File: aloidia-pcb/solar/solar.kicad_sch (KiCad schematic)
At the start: 4 parts, among them J1 S2B-PH-SM4-TB(LF)(SN)

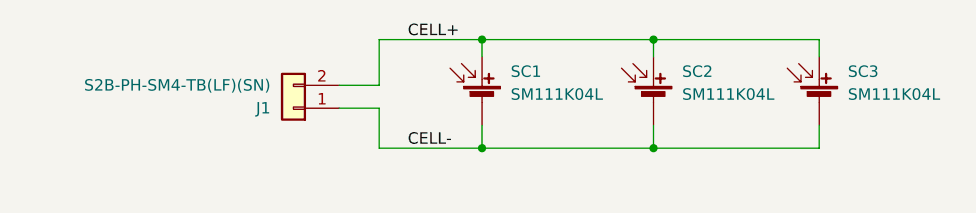
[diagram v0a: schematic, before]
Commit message: Changed connectors to jst-sh
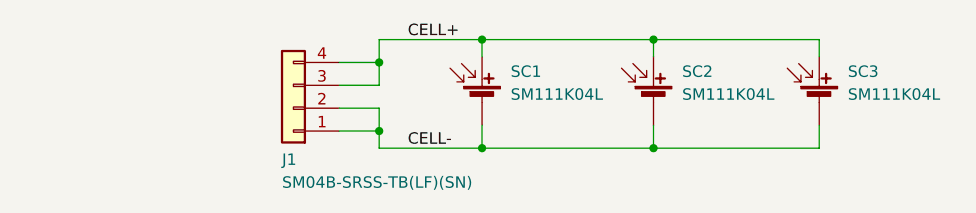
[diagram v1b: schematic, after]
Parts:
- removed J1: S2B-PH-SM4-TB(LF)(SN), Connector_JST:JST_PH_S2B-PH-SM4-TB_1x02-1MP_P2.00mm_Horizontal, symbol Connector_Generic:Conn_01x02
- added J1: SM04B-SRSS-TB(LF)(SN), Connector_JST:JST_SH_SM04B-SRSS-TB_1x04-1MP_P1.00mm_Horizontal, symbol Connector_Generic:Conn_01x04
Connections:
- net CELL+: now also J1.3 (Pin_3), J1.4 (Pin_4)
- net CELL-: now also J1.1 (Pin_1), J1.2 (Pin_2)
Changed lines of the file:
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@@
     (comment 2 "Author: Vincent Nguyen")
+  )
+  (junction (at 130.81 94.615) (diameter 0) (color 0 0 0 0)
+  )
+  (junction (at 130.81 102.235) (diameter 0) (color 0 0 0 0)
   )
   (junction (at 142.24 92.075) (diameter 0) (color 0 0 0 0)
@@
   )
   (junction (at 161.29 104.14) (diameter 0) (color 0 0 0 0)
+  )
+  (wire (pts (xy 126.365 102.235) (xy 130.81 102.235))
+    (stroke (width 0) (type default) (color 0 0 0 0))
   )
   (wire (pts (xy 161.29 92.075) (xy 179.705 92.075))
@@
     (stroke (width 0) (type default) (color 0 0 0 0))
   )
-  (wire (pts (xy 130.81 97.155) (xy 130.81 92.075))
+  (wire (pts (xy 130.81 92.075) (xy 130.81 94.615))
     (stroke (width 0) (type default) (color 0 0 0 0))
   )
@@
   )
   (wire (pts (xy 179.705 101.6) (xy 179.705 104.14))
+    (stroke (width 0) (type default) (color 0 0 0 0))
+  )
+  (wire (pts (xy 126.365 94.615) (xy 130.81 94.615))
     (stroke (width 0) (type default) (color 0 0 0 0))
   )
@@
     (stroke (width 0) (type default) (color 0 0 0 0))
   )
-  (wire (pts (xy 130.81 99.695) (xy 130.81 104.14))
+  (wire (pts (xy 130.81 99.695) (xy 130.81 102.235))
+    (stroke (width 0) (type default) (color 0 0 0 0))
+  )
+  (wire (pts (xy 130.81 94.615) (xy 130.81 97.155))
+    (stroke (width 0) (type default) (color 0 0 0 0))
+  )
+  (wire (pts (xy 130.81 102.235) (xy 130.81 104.14))
     (stroke (width 0) (type default) (color 0 0 0 0))
   )
@@
     (pin "2")
   )
-  (symbol (lib_id "Connector_Generic:Conn_01x02") (at 121.285 99.695 180) (unit 1)
-    (in_bom yes) (on_board yes) (fields_autoplaced)
-    (property "Reference" "J1" (id 0) (at 118.745 99.6951 0)
-      (effects (font (size 1.27 1.27)) (justify left))
+  (symbol (lib_id "Connector_Generic:Conn_01x04") (at 121.285 99.695 180) (unit 1)
+    (in_bom yes) (on_board yes)
+    (property "Reference" "J1" (id 0) (at 120.015 105.41 0)
+      (effects (font (size 1.27 1.27)) (justify right))
     )
-    (property "Value" "S2B-PH-SM4-TB(LF)(SN)" (id 1) (at 118.745 97.1551 0)
-      (effects (font (size 1.27 1.27)) (justify left))
+    (property "Value" "SM04B-SRSS-TB(LF)(SN)" (id 1) (at 120.015 107.95 0)
+      (effects (font (size 1.27 1.27)) (justify right))
     )
-    (property "Footprint" "Connector_JST:JST_PH_S2B-PH-SM4-TB_1x02-1MP_P2.00mm_Horizontal" (id 2) (at 121.285 99.695 0)
+    (property "Footprint" "Connector_JST:JST_SH_SM04B-SRSS-TB_1x04-1MP_P1.00mm_Horizontal" (id 2) (at 121.285 99.695 0)
       (effects (font (size 1.27 1.27)) hide)
     )
@@
     (pin "1")
     (pin "2")
+    (pin "3")
+    (pin "4")
   )
   (symbol (lib_id "Device:Solar_Cell") (at 179.705 99.06 0) (unit 1)
@@
   )
   (symbol_instances
-    (path "/dd7481c5-e18b-4131-a3de-fb23c40c0bf5"
-      (reference "J1") (unit 1) (value "S2B-PH-SM4-TB(LF)(SN)") (footprint "Connector_JST:JST_PH_S2B-PH-SM4-TB_1x02-1MP_P2.00mm_Horizontal")
+    (path "/b829a62e-8f9e-48dc-83b9-c62a484abb2a"
+      (reference "J1") (unit 1) (value "SM04B-SRSS-TB(LF)(SN)") (footprint "Connector_JST:JST_SH_SM04B-SRSS-TB_1x04-1MP_P1.00mm_Horizontal")
     )
     (path "/aebe1b36-46d1-4070-bb5f-6bb872604111"
